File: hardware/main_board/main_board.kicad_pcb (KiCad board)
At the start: 4 copper layers, 225.9 x 135 mm, 86 parts, among them J1 +5v in, J10 uart, J11 input 4, J12 input 5, J14 +5v out, J16 input 6, J17 input 7, J19 rgb output, J20 ypbpr output, J3 input 0, J4 input 1, J5 icsp, J7 input 2, J8 input 3, SW1 rgb/ypbpr, SW10 prev, SW11 next, SW12 csync/rgbs, SW13 csync/rgbs, SW14 csync/rgbs, SW15 csync/rgbs, SW16 csync/rgbs, SW17 csync/rgbs, SW18 csync/rgbs, SW19 csync/rgbs, SW2 rgb/ypbpr, SW20 csync/rgbs, SW3 rgb/ypbpr, SW4 rgb/ypbpr, SW5 rgb/ypbpr, SW6 rgb/ypbpr, SW7 rgb/ypbpr, SW8 rgb/ypbpr, U1 ATmega328PB-A, U10 SN74CBT3244CPW, U11 SN74CBT3244CPW, U12 SN74CBT3244CPW, U13 SN74CBT3244CPW, U14 74HC238, U15 74HC238, U3 SN74CBT3244CPW, U4 SN74CBT3244CPW, U5 74HC138, U6 74HC04, U7 SN74CBT3244CPW, U8 SN74CBT3244CPW, U9 SN74CBT3244CPW

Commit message: #5: Moved prev/next buttons closer to the edge for ease of use. Fixed issue with mounting hole positions. They are now consistently 10mm from their nearest edges.
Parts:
- moved SW11 88.7 mm to (222.3, 25.6)
- moved SW10 88.7 mm to (233.6, 25.6)
- moved H1 87.8 mm to (45.8, 33.4)
- moved C13 87.1 mm to (130.2, 138.2)
- moved C8 87.1 mm to (203.6, 138.2)
- moved C16 87.1 mm to (129.2, 51.4)
- moved C10 87.1 mm to (185.4, 138.2)
- moved C11 87.1 mm to (167.0, 138.2)
- moved C12 87.1 mm to (148.6, 138.2)
- moved C14 87.1 mm to (112.8, 137.3)
- moved C15 87.1 mm to (93.6, 138.2)
- moved C18 87.1 mm to (66.0, 132.4)
- moved C3 87.1 mm to (46.5, 135.4)
- moved C4 87.1 mm to (44.8, 134.2)
- moved C7 87.1 mm to (221.8, 138.2)
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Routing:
- net PIN_BTNPREV: track 87.4 -> 89.7 mm
- net PIN_BTNNEXT: track 82.4 -> 84.7 mm

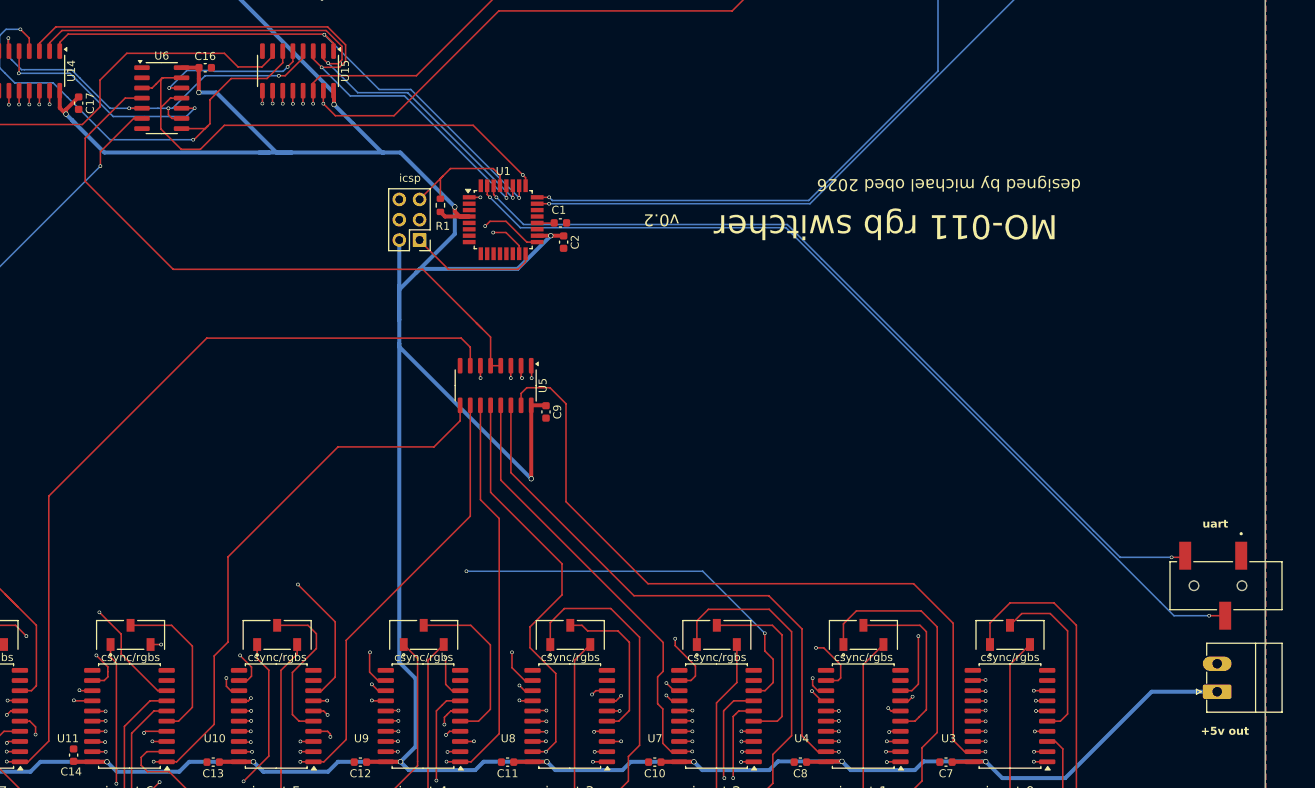
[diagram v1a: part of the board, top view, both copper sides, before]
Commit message: #5: Fix missing C19. Minor artwork updates. Actually, why not let the +5v connector be in/out?
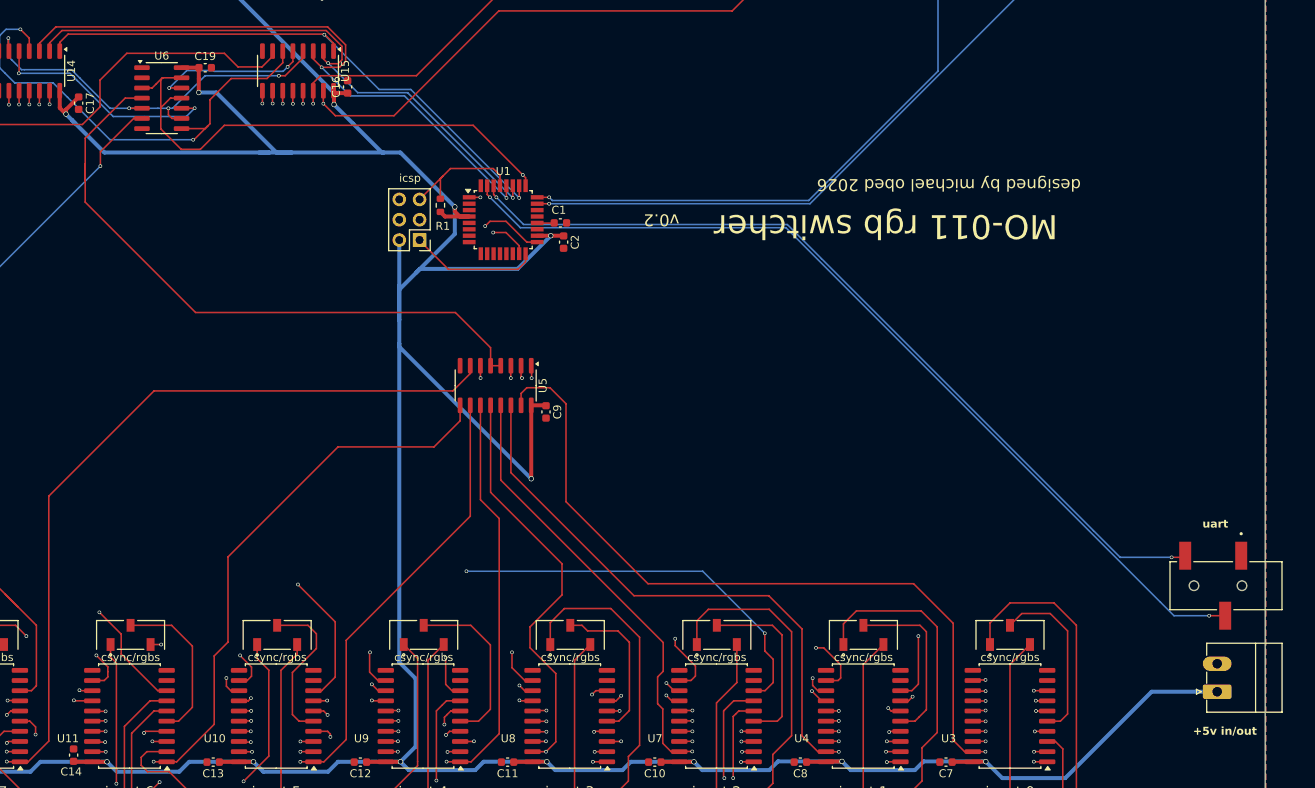
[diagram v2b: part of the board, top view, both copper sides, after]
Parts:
- added C19: 100n, Capacitor_SMD:C_0603_1608Metric, F.Cu at (129.2, 51.4)
- J14: value +5v out -> +5v in/out
- moved C16 18.0 mm to (147.0, 53.8), turned to 90 degrees
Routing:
- net OutputEnable7Inv: track 108.8 -> 105.1 mm
- net Net-(U5-~{E0}): track 79.2 -> 81.1 mm
- net +5V: track 704.0 -> 705.9 mm

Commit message: #5: Properly handle unused NOT gate. Prune unused symbol/footprint libs.
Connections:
- U6 pad 1: (no net) -> GND
- U6 pad 2: (no net) -> unconnected-(U6-Pad2)
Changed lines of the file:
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@@
 	(paper "A4")
 	(title_block
-		(title "MO-011 rgb switcher")
+		(title "MO-011 rgb switcher (main board)")
 		(date "2025-01-21")
 		(rev "v0.2")
@@
 	(net 197 "Net-(SW20-A)")
 	(net 198 "Net-(SW20-C)")
+	(net 199 "unconnected-(U6-Pad2)")
 	(footprint "MountingHole:MountingHole_4.3mm_M4_ISO14580_Pad"
 		(layer "F.Cu")
@@
 			(layers "F.Cu" "F.Mask" "F.Paste")
 			(roundrect_rratio 0.25)
+			(net 2 "GND")
+			(pintype "input")
 		)
 		(pad "2" smd roundrect
@@
 			(layers "F.Cu" "F.Mask" "F.Paste")
 			(roundrect_rratio 0.25)
+			(net 199 "unconnected-(U6-Pad2)")
+			(pintype "output+no_connect")
 		)
 		(pad "3" smd roundrect
